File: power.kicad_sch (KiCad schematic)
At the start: 64 parts, among them Q1 CSD17303Q5, Q2 CSD17573Q5B, U1 LMR54410, U11 RT9080-33GJ5, U4 LM27402, U5 MIC5504, U6 DS4432U+, U6 INA219AID

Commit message: small schematic cleanup
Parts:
- R10, R9: value 7.87K -> 7.87k
- R107: value 20K -> 20k
- R110: value 4.02K -> 4.02k
- R111: value 140R -> 140
- R112: value 115K -> 115k
- R113: value 22.1K -> 22.1k
- R114, R4: value 11.8K -> 11.8k
- R5: value 2.21R -> 2.21
- R6: value 3.83K -> 3.83k
- R8: value 887R -> 887
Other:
- moved on the sheet: R10
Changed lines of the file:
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@@
     (stroke (width 0) (type default))
   )
-  (wire (pts (xy 186.69 62.23) (xy 186.69 72.39))
+  (wire (pts (xy 186.69 66.675) (xy 186.69 72.39))
     (stroke (width 0) (type default))
   )
@@
     (stroke (width 0) (type default))
   )
-  (wire (pts (xy 186.69 52.07) (xy 186.69 54.61))
+  (wire (pts (xy 186.69 52.07) (xy 186.69 59.055))
     (stroke (width 0) (type default))
   )
@@
   (symbol (lib_id "Device:C") (at 30.48 58.42 180) (unit 1)
     (in_bom yes) (on_board yes) (dnp no)
-    (property "Reference" "C2" (at 27.305 55.88 0)
+    (property "Reference" "C2" (at 28.575 55.88 0)
       (effects (font (size 1.27 1.27)) (justify left))
     )
@@
   (symbol (lib_id "Device:R_US") (at 101.6 36.83 0) (unit 1)
     (in_bom yes) (on_board yes) (dnp no)
-    (property "Reference" "R5" (at 95.25 36.195 0)
-      (effects (font (size 1.27 1.27)) (justify left))
-    )
-    (property "Value" "2.21R" (at 93.98 38.735 0)
+    (property "Reference" "R5" (at 97.155 36.195 0)
+      (effects (font (size 1.27 1.27)) (justify left))
+    )
+    (property "Value" "2.21" (at 95.25 38.735 0)
       (effects (font (size 1.27 1.27)) (justify left))
     )
@@
       (effects (font (size 1.27 1.27)))
     )
-    (property "Value" "3.83K" (at 140.335 82.55 90)
+    (property "Value" "3.83k" (at 140.335 82.55 90)
       (effects (font (size 1.27 1.27)))
     )
@@
       (effects (font (size 1.27 1.27)))
     )
-    (property "Value" "20K" (at 191.135 64.77 0)
+    (property "Value" "20k" (at 191.135 64.77 0)
       (effects (font (size 1.27 1.27)))
     )
@@
       (effects (font (size 1.27 1.27)))
     )
-    (property "Value" "140R" (at 208.28 68.58 0)
+    (property "Value" "140" (at 207.645 68.58 0)
       (effects (font (size 1.27 1.27)))
     )
@@
   (symbol (lib_id "Device:C") (at 78.74 86.995 0) (unit 1)
     (in_bom yes) (on_board yes) (dnp no)
-    (property "Reference" "C14" (at 74.93 83.82 0)
+    (property "Reference" "C14" (at 74.295 83.82 0)
       (effects (font (size 1.27 1.27)) (justify left))
     )
@@
   )
   (symbol (lib_id "Device:C") (at 56.515 31.75 0) (unit 1)
-    (in_bom yes) (on_board yes) (dnp no) (fields_autoplaced)
-    (property "Reference" "C6" (at 60.325 30.48 0)
-      (effects (font (size 1.27 1.27)) (justify left))
-    )
-    (property "Value" "22uF" (at 60.325 33.02 0)
+    (in_bom yes) (on_board yes) (dnp no)
+    (property "Reference" "C6" (at 59.69 30.48 0)
+      (effects (font (size 1.27 1.27)) (justify left))
+    )
+    (property "Value" "22uF" (at 59.69 33.02 0)
       (effects (font (size 1.27 1.27)) (justify left))
     )
@@
       (effects (font (size 1.27 1.27)))
     )
-    (property "Value" "7.87K" (at 168.275 60.325 0)
+    (property "Value" "7.87k" (at 168.275 60.325 0)
       (effects (font (size 1.27 1.27)))
     )
@@
       (effects (font (size 1.27 1.27)) (justify left))
     )
-    (property "Value" "1uF" (at 36.195 89.535 0)
+    (property "Value" "1uF" (at 36.83 89.535 0)
       (effects (font (size 1.27 1.27)) (justify left))
     )
@@
       (effects (font (size 1.27 1.27)) (justify left))
     )
-    (property "Value" "11.8K" (at 86.995 88.265 0)
+    (property "Value" "11.8k" (at 86.995 88.265 0)
       (effects (font (size 1.27 1.27)) (justify left))
     )
@@
     )
   )
-  (symbol (lib_id "Device:R_US") (at 186.69 58.42 180) (unit 1)
-    (in_bom yes) (on_board yes) (dnp no)
-    (property "Reference" "R10" (at 183.515 57.785 0)
-      (effects (font (size 1.27 1.27)))
-    )
-    (property "Value" "7.87K" (at 182.245 60.325 0)
-      (effects (font (size 1.27 1.27)))
-    )
-    (property "Footprint" "Resistor_SMD:R_0402_1005Metric" (at 185.674 58.166 90)
-      (effects (font (size 1.27 1.27)) hide)
-    )
-    (property "Datasheet" "~" (at 186.69 58.42 0)
-      (effects (font (size 1.27 1.27)) hide)
-    )
-    (property "DK" "311-7.87KLRCT-ND" (at 186.69 58.42 0)
-      (effects (font (size 1.27 1.27)) hide)
-    )
-    (property "PARTNO" "RC0402FR-077K87L" (at 186.69 58.42 0)
+  (symbol (lib_id "Device:R_US") (at 186.69 62.865 180) (unit 1)
+    (in_bom yes) (on_board yes) (dnp no)
+    (property "Reference" "R10" (at 183.515 62.23 0)
+      (effects (font (size 1.27 1.27)))
+    )
+    (property "Value" "7.87k" (at 182.245 64.77 0)
+      (effects (font (size 1.27 1.27)))
+    )
+    (property "Footprint" "Resistor_SMD:R_0402_1005Metric" (at 185.674 62.611 90)
+      (effects (font (size 1.27 1.27)) hide)
+    )
+    (property "Datasheet" "~" (at 186.69 62.865 0)
+      (effects (font (size 1.27 1.27)) hide)
+    )
+    (property "DK" "311-7.87KLRCT-ND" (at 186.69 62.865 0)
+      (effects (font (size 1.27 1.27)) hide)
+    )
+    (property "PARTNO" "RC0402FR-077K87L" (at 186.69 62.865 0)
       (effects (font (size 1.27 1.27)) hide)
     )
@@
       (effects (font (size 1.27 1.27)))
     )
-    (property "Value" "887R" (at 165.1 54.61 90)
+    (property "Value" "887" (at 165.1 54.61 90)
       (effects (font (size 1.27 1.27)))
     )
@@
       (effects (font (size 1.27 1.27)) (justify left))
     )
-    (property "Value" "22.1K" (at 111.76 190.5 0)
+    (property "Value" "22.1k" (at 111.76 190.5 0)
       (effects (font (size 1.27 1.27)) (justify left))
     )
@@
       (effects (font (size 1.27 1.27)) (justify left))
     )
-    (property "Value" "115K" (at 111.76 179.07 0)
+    (property "Value" "115k" (at 111.76 179.07 0)
       (effects (font (size 1.27 1.27)) (justify left))
     )
@@
       (effects (font (size 1.27 1.27)))
     )
-    (property "Value" "4.02K" (at 190.5 88.265 0)
+    (property "Value" "4.02k" (at 190.5 88.265 0)
       (effects (font (size 1.27 1.27)))
     )
@@
       (effects (font (size 1.27 1.27)) (justify left))
     )
-    (property "Value" "11.8K" (at 60.96 88.9 0)
-      (effects (font (size 1.27 1.27)) (justify left))
-    )
+    (property "Value" "11.8k" (at 60.96 88.9 0)
+      (effects (font (size 1.27 1.27)) (justify left))
+    )

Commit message: adjust some values on the BOM
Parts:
- C1: DK 1276-3363-1-ND -> 1276-1101-1-ND; PARTNO CL32A106KBJNNNE -> CL32A226KAJNNNE
- L2: DK 732-11205-1-ND -> 732-11745-1-ND; PARTNO 74438357082 -> 78438357082
- R6: DK 311-1.33KLRCT-ND -> 311-3.83KLRCT-ND; PARTNO RC0402FR-071K33L -> RC0402FR-073K83L
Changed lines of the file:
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@@
       (effects (font (size 1.27 1.27)) hide)
     )
-    (property "DK" "311-1.33KLRCT-ND" (at 140.335 80.01 0)
-      (effects (font (size 1.27 1.27)) hide)
-    )
-    (property "PARTNO" "RC0402FR-071K33L" (at 140.335 80.01 0)
+    (property "DK" "311-3.83KLRCT-ND" (at 140.335 80.01 0)
+      (effects (font (size 1.27 1.27)) hide)
+    )
+    (property "PARTNO" "RC0402FR-073K83L" (at 140.335 80.01 0)
       (effects (font (size 1.27 1.27)) hide)
     )
@@
       (effects (font (size 1.27 1.27)) hide)
     )
-    (property "DK" "1276-3363-1-ND" (at 45.72 31.75 0)
-      (effects (font (size 1.27 1.27)) hide)
-    )
-    (property "PARTNO" "CL32A106KBJNNNE" (at 45.72 31.75 0)
+    (property "DK" "1276-1101-1-ND" (at 45.72 31.75 0)
+      (effects (font (size 1.27 1.27)) hide)
+    )
+    (property "PARTNO" "CL32A226KAJNNNE" (at 45.72 31.75 0)
       (effects (font (size 1.27 1.27)) hide)
     )
@@
       (effects (font (size 1.27 1.27)) hide)
     )
-    (property "PARTNO" "74438357082" (at 100.965 170.815 90)
-      (effects (font (size 1.27 1.27)) hide)
-    )
-    (property "DK" "732-11205-1-ND" (at 100.965 170.815 90)
-      (effects (font (size 1.27 1.27)) hide)
-    )
+    (property "PARTNO" "78438357082" (at 100.965 170.815 90)
+      (effects (font (size 1.27 1.27)) hide)
+    )
+    (property "DK" "732-11745-1-ND" (at 100.965 170.815 90)
+      (effects (font (size 1.27 1.27)) hide)
+    )

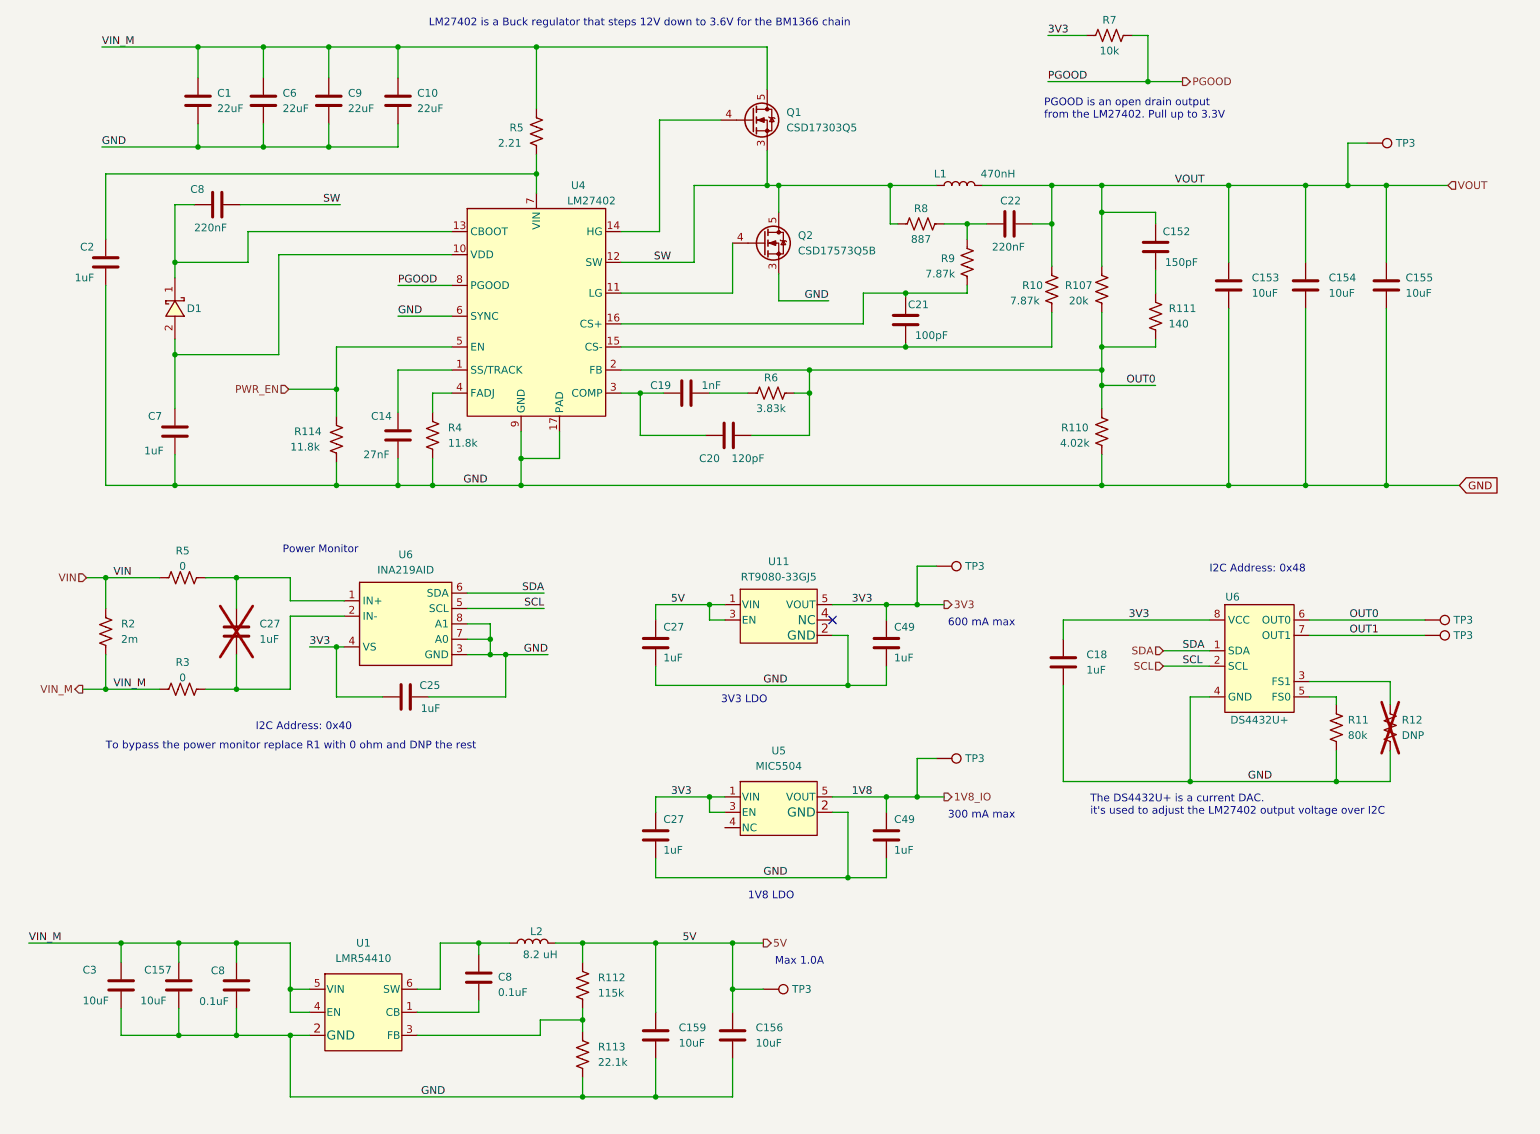
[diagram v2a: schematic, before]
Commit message: first draft of new power supply schematic using TPS546D24
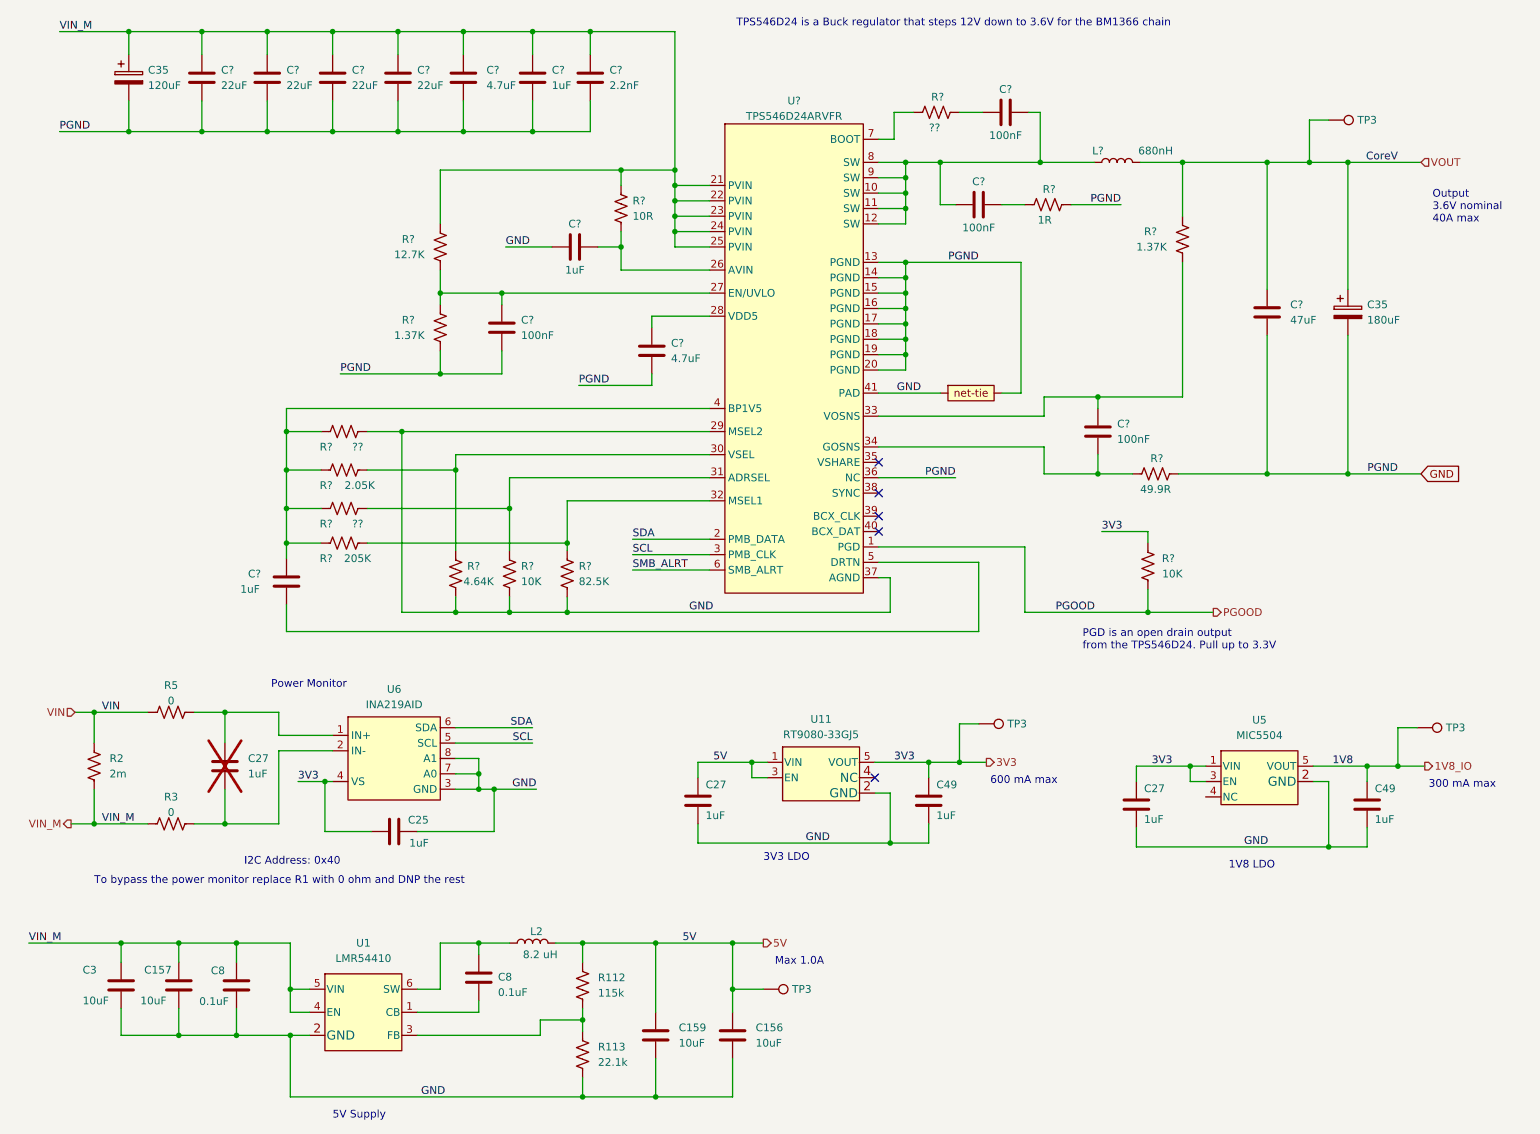
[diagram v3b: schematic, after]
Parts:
- removed C1, C10, C6, C9: 22uF, Capacitor_SMD:C_1210_3225Metric, symbol Device:C
- removed C14: 27nF, Capacitor_SMD:C_0402_1005Metric, symbol Device:C
- removed C152: 150pF, Capacitor_SMD:C_0402_1005Metric, symbol Device:C
- removed C153, C154, C155: 10uF, Capacitor_SMD:C_0805_2012Metric, symbol Device:C
- removed C18: 1uF, Capacitor_SMD:C_0402_1005Metric, symbol Device:C
- removed C19: 1nF, Capacitor_SMD:C_0402_1005Metric, symbol Device:C
- removed C2: 1uF, Capacitor_SMD:C_0805_2012Metric, symbol Device:C
- removed C20: 120pF, Capacitor_SMD:C_0402_1005Metric, symbol Device:C
- removed C21: 100pF, Capacitor_SMD:C_0402_1005Metric, symbol Device:C
- removed C22: 220nF, Capacitor_SMD:C_0402_1005Metric, symbol Device:C
- removed C7: 1uF, Capacitor_SMD:C_0603_1608Metric, symbol Device:C
- removed C8: 220nF, Capacitor_SMD:C_0603_1608Metric, symbol Device:C
- removed D1: XBS104S13R-G, Diode_SMD:D_SOD-323, symbol lcsc:SS310_C85658
- removed L1: 470nH, bitaxe:744373580047, symbol Device:L
- removed Q1: CSD17303Q5, bitaxe:SON-Q5-MOSFET, symbol bitaxe:Q_NMOS_CSD16340Q3
- removed Q2: CSD17573Q5B, bitaxe:SON-Q5-MOSFET, symbol bitaxe:Q_NMOS_CSD17573Q5B
- removed R10, R9: 7.87k, Resistor_SMD:R_0402_1005Metric, symbol Device:R_US
- removed R107: 20k, Resistor_SMD:R_0402_1005Metric, symbol Device:R_US
- removed R11: 80k, Resistor_SMD:R_0402_1005Metric, symbol Device:R_US
- removed R110: 4.02k, Resistor_SMD:R_0402_1005Metric, symbol Device:R_US
- removed R111: 140, Resistor_SMD:R_0402_1005Metric, symbol Device:R_US
- removed R114, R4: 11.8k, Resistor_SMD:R_0402_1005Metric, symbol Device:R_US
- removed R12: DNP, Resistor_SMD:R_0402_1005Metric, symbol Device:R_US
- removed R5: 2.21, Resistor_SMD:R_0402_1005Metric, symbol Device:R_US
- removed R6: 3.83k, Resistor_SMD:R_0402_1005Metric, symbol Device:R_US
- removed R7: 10k, Resistor_SMD:R_0402_1005Metric, symbol Device:R_US
- removed R8: 887, Resistor_SMD:R_0402_1005Metric, symbol Device:R_US
- removed TP3 (x3): TestPoint, TestPoint:TestPoint_Pad_D1.0mm, symbol Connector:TestPoint
- removed U4: LM27402, bitaxe:SQB16A, symbol bitaxe:LM27402
- removed U6: DS4432U+, Package_SO:TSSOP-8_3x3mm_P0.65mm, symbol bitaxe:DS4432U+
- added C35: 180uF, Capacitor_SMD:CP_Elec_6.3x7.7, symbol Device:C_Polarized
- added C35: 120uF, Capacitor_SMD:CP_Elec_6.3x7.7, symbol Device:C_Polarized
- added C? (x2): 100nF, Capacitor_SMD:C_0402_1005Metric, symbol Device:C
- added C? (x4): 22uF, Capacitor_SMD:C_1210_3225Metric, symbol Device:C
- added C? (x2): 100nF, Capacitor_SMD:C_1210_3225Metric, symbol Device:C
- added C?: 47uF, Capacitor_SMD:C_1210_3225Metric, symbol Device:C
- added C?: 2.2nF, Capacitor_SMD:C_1210_3225Metric, symbol Device:C
- added C? (x2): 1uF, Capacitor_SMD:C_1210_3225Metric, symbol Device:C
- added C?: 1uF, Capacitor_SMD:C_0402_1005Metric, symbol Device:C
- added C? (x2): 4.7uF, Capacitor_SMD:C_1210_3225Metric, symbol Device:C
- added L?: 680nH, bitaxe:744373580047, symbol Device:L
- added R? (x3): ??, Resistor_SMD:R_0402_1005Metric, symbol Device:R_US
- added R? (x2): 10K, Resistor_SMD:R_0402_1005Metric, symbol Device:R_US
- added R?: 49.9R, Resistor_SMD:R_0402_1005Metric, symbol Device:R_US
- added R?: 1R, Resistor_SMD:R_0402_1005Metric, symbol Device:R_US
- added R?: 10R, Resistor_SMD:R_0402_1005Metric, symbol Device:R_US
- added R?: 205K, Resistor_SMD:R_0402_1005Metric, symbol Device:R_US
- added R? (x2): 1.37K, Resistor_SMD:R_0402_1005Metric, symbol Device:R_US
- added R?: 4.64K, Resistor_SMD:R_0402_1005Metric, symbol Device:R_US
- added R?: 82.5K, Resistor_SMD:R_0402_1005Metric, symbol Device:R_US
- added R?: 12.7K, Resistor_SMD:R_0402_1005Metric, symbol Device:R_US
- added R?: 2.05K, Resistor_SMD:R_0402_1005Metric, symbol Device:R_US
- added T1: net-tie, symbol bitaxe:net-tie
- added TP3: TestPoint, TestPoint:TestPoint_Pad_D1.0mm, symbol Connector:TestPoint
- added U?: TPS546D24ARVFR, symbol bitaxe:TPS546D24
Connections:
- net 3V3: now also R?.2
- net GND: now also C35.2, C35.2, C?.1, C?.2, C?.2, C?.2, C?.2, C?.2, C?.2, C?.2, C?.2, C?.2, C?.2, R?.2, R?.2, R?.2, R?.2, R?.2, R?.2, R?.2, T1., U?.13 (PGND), U?.14 (PGND), U?.15 (PGND), U?.16 (PGND), U?.17 (PGND), U?.18 (PGND), U?.19 (PGND), U?.20 (PGND), U?.29 (MSEL2), U?.36 (NC), U?.37 (AGND), U?.41 (PAD)
- net PGOOD: now also R?.1, U?.1 (PGD)
- net SCL: now also U?.3 (PMB_CLK)
- net SDA: now also U?.2 (PMB_DATA)
- net VIN_M: now also C35.1, C?.1, C?.1, C?.1, C?.1, C?.1, C?.1, C?.1, R?.1, R?.1, U?.21 (PVIN), U?.22 (PVIN), U?.23 (PVIN), U?.24 (PVIN), U?.25 (PVIN)
- net VOUT: now also C35.1, C?.1, L?.2, R?.1, TP3.1
- new net: C?.1, R?.2
- new net: C?.1, C?.2, L?.1, U?.10 (SW), U?.11 (SW), U?.12 (SW), U?.8 (SW), U?.9 (SW)
- new net: C?.1, R?.1, R?.1, R?.1, R?.1, U?.4 (BP1V5)
- new net: R?.1, R?.2, U?.31 (ADRSEL)
- new net: C?.1, R?.2, U?.33 (VOSNS)
- new net: C?.2, R?.1, U?.34 (GOSNS)
- new net: C?.2, R?.1
- new net: C?.2, R?.2, U?.26 (AVIN)
- new net: R?.1, R?.2, U?.32 (MSEL1)
- new net: C?.1, R?.1, R?.2, U?.27 (EN/UVLO)
- new net: R?.1, R?.2, U?.30 (VSEL)
- new net: R?.1, U?.7 (BOOT)
- new net: C?.1, U?.28 (VDD5)
- new net: C?.2, U?.5 (DRTN)
- new net SMB_ALRT: U?.6 (SMB_ALRT)
- no-connect marks 1 -> 5
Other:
- note added: "5V Supply"
- note added: "Output 3.6V nominal 40A max"
- note added: "PGD is an open drain output from the TPS546D24. Pull up to 3.3V"
- note added: "TPS546D24 is a Buck regulator that steps 12V down to 3.6V for the BM1366 chain"
- note removed: "I2C Address: 0x48"
- note removed: "LM27402 is a Buck regulator that steps 12V down to 3.6V for the BM1366 chain"
- note removed: "PGOOD is an open drain output from the LM27402. Pull up to 3.3V"
- note removed: "The DS4432U+ is a current DAC. it's used to adjust the LM27402 output voltage over I2C"
- moved on the sheet: C25, C27, C49, R2, R3, R5, TP3, U11, U5, U6
